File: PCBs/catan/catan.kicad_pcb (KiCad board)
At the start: 2 copper layers, 95.3 x 110 mm, 65 parts, among them J1 Conn_01x04_Female, J2 Conn_01x06_Male, SW1 SW_MEC_5E, SW10 SW_MEC_5E, SW11 SW_MEC_5E, SW2 SW_MEC_5E, SW3 SW_MEC_5E, SW4 SW_MEC_5E, SW5 SW_MEC_5E, SW6 SW_MEC_5E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

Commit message: wire buttons
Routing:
- net Net-(R25-Pad2): track 3.07 -> 84.9 mm
- net Net-(R24-Pad2): track 2.54 -> 59.8 mm
- net Net-(R3-Pad2): track 4.34 -> 57.9 mm
- net Net-(R4-Pad2): track 3.44 -> 54.3 mm
- net Net-(R5-Pad2): track 4.86 -> 39.1 mm
- net Net-(R6-Pad2): track 2.54 -> 29.4 mm
- net Net-(R23-Pad2): track 3.59 -> 28.5 mm
- net Net-(R27-Pad2): track 3.33 -> 27.6 mm
- net GND: track 633.6 -> 649.8 mm
- net Net-(R7-Pad2): track 6.40 -> 18.8 mm
- net Net-(R26-Pad2): track 3.33 -> 15.0 mm
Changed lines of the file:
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@@
     (thickness 1.6)
     (drawings 12)
-    (tracks 281)
+    (tracks 330)
     (zones 0)
     (modules 65)
@@
   (segment (start 139.7 116.205) (end 134.129999 110.634999) (width 0.25) (layer B.Cu) (net 1))
   (segment (start 119.38 93.345) (end 131.445 93.345) (width 0.25) (layer B.Cu) (net 1))
+  (segment (start 102.87 92.075) (end 102.87 94.615) (width 0.25) (layer B.Cu) (net 1))
+  (segment (start 102.87 94.615) (end 102.87 97.155) (width 0.25) (layer B.Cu) (net 1))
+  (segment (start 102.87 97.155) (end 102.87 99.695) (width 0.25) (layer B.Cu) (net 1))
+  (segment (start 103.995001 103.649999) (end 102.87 104.775) (width 0.25) (layer B.Cu) (net 1))
+  (segment (start 103.995001 100.820001) (end 103.995001 103.649999) (width 0.25) (layer B.Cu) (net 1))
+  (segment (start 102.87 99.695) (end 103.995001 100.820001) (width 0.25) (layer B.Cu) (net 1))
+  (segment (start 110.49 92.075) (end 110.49 94.615) (width 0.25) (layer B.Cu) (net 1))
   (segment (start 90.805 63.5) (end 90.805 71.12) (width 0.25) (layer B.Cu) (net 2))
   (segment (start 86.995 74.93) (end 90.805 71.12) (width 0.25) (layer B.Cu) (net 2))
@@
   (segment (start 158.115 85.725) (end 159.385 86.995) (width 0.25) (layer B.Cu) (net 41))
   (segment (start 158.115 83.185) (end 158.115 85.725) (width 0.25) (layer B.Cu) (net 41))
+  (segment (start 112.000001 77.229999) (end 110.49 78.74) (width 0.25) (layer F.Cu) (net 41))
+  (segment (start 136.065001 77.229999) (end 112.000001 77.229999) (width 0.25) (layer F.Cu) (net 41))
+  (segment (start 145.830002 86.995) (end 136.065001 77.229999) (width 0.25) (layer F.Cu) (net 41))
+  (segment (start 159.385 86.995) (end 145.830002 86.995) (width 0.25) (layer F.Cu) (net 41))
   (segment (start 158.115 74.295) (end 158.75 74.93) (width 0.25) (layer B.Cu) (net 42))
   (segment (start 158.115 71.755) (end 158.115 74.295) (width 0.25) (layer B.Cu) (net 42))
+  (segment (start 155.970002 76.2) (end 110.49 76.2) (width 0.25) (layer F.Cu) (net 42))
+  (segment (start 158.115 74.055002) (end 155.970002 76.2) (width 0.25) (layer F.Cu) (net 42))
+  (segment (start 158.115 71.755) (end 158.115 74.055002) (width 0.25) (layer F.Cu) (net 42))
   (segment (start 137.16 59.055) (end 139.7 61.595) (width 0.25) (layer B.Cu) (net 43))
   (segment (start 137.16 57.785) (end 137.16 59.055) (width 0.25) (layer B.Cu) (net 43))
+  (segment (start 139.7 61.595) (end 127.635 73.66) (width 0.25) (layer F.Cu) (net 43))
+  (segment (start 127.635 73.66) (end 110.49 73.66) (width 0.25) (layer F.Cu) (net 43))
   (segment (start 121.92 50.165) (end 119.38 50.165) (width 0.25) (layer B.Cu) (net 44))
+  (segment (start 119.139999 62.470001) (end 110.49 71.12) (width 0.25) (layer F.Cu) (net 44))
+  (segment (start 119.139999 58.264999) (end 119.139999 62.470001) (width 0.25) (layer F.Cu) (net 44))
+  (segment (start 121.034997 56.370001) (end 119.139999 58.264999) (width 0.25) (layer F.Cu) (net 44))
+  (segment (start 121.825001 56.370001) (end 121.034997 56.370001) (width 0.25) (layer F.Cu) (net 44))
+  (segment (start 122.769999 51.014999) (end 122.769999 55.425003) (width 0.25) (layer F.Cu) (net 44))
+  (segment (start 122.769999 55.425003) (end 121.825001 56.370001) (width 0.25) (layer F.Cu) (net 44))
+  (segment (start 121.92 50.165) (end 122.769999 51.014999) (width 0.25) (layer F.Cu) (net 44))
   (segment (start 100.965 64.135) (end 104.14 60.96) (width 0.25) (layer B.Cu) (net 45))
   (segment (start 99.06 64.135) (end 100.965 64.135) (width 0.25) (layer B.Cu) (net 45))
+  (segment (start 101.744999 69.994999) (end 102.87 71.12) (width 0.25) (layer F.Cu) (net 45))
+  (segment (start 101.744999 68.039999) (end 101.744999 69.994999) (width 0.25) (layer F.Cu) (net 45))
+  (segment (start 102.619997 67.165001) (end 101.744999 68.039999) (width 0.25) (layer F.Cu) (net 45))
+  (segment (start 103.930001 67.165001) (end 102.619997 67.165001) (width 0.25) (layer F.Cu) (net 45))
+  (segment (start 104.14 66.955002) (end 103.930001 67.165001) (width 0.25) (layer F.Cu) (net 45))
+  (segment (start 104.14 60.96) (end 104.14 66.955002) (width 0.25) (layer F.Cu) (net 45))
   (segment (start 90.17 93.345) (end 92.71 95.885) (width 0.25) (layer B.Cu) (net 61))
+  (segment (start 91.345001 85.184999) (end 102.87 73.66) (width 0.25) (layer F.Cu) (net 61))
+  (segment (start 91.345001 92.169999) (end 91.345001 85.184999) (width 0.25) (layer F.Cu) (net 61))
+  (segment (start 90.17 93.345) (end 91.345001 92.169999) (width 0.25) (layer F.Cu) (net 61))
   (segment (start 110.49 116.205) (end 110.49 118.745) (width 0.25) (layer B.Cu) (net 62))
+  (segment (start 102.87 76.2) (end 94.615 84.455) (width 0.25) (layer F.Cu) (net 62))
+  (segment (start 105.739989 113.994989) (end 110.49 118.745) (width 0.25) (layer F.Cu) (net 62))
+  (segment (start 97.739987 113.994989) (end 105.739989 113.994989) (width 0.25) (layer F.Cu) (net 62))
+  (segment (start 94.615 110.870002) (end 97.739987 113.994989) (width 0.25) (layer F.Cu) (net 62))
+  (segment (start 94.615 84.455) (end 94.615 110.870002) (width 0.25) (layer F.Cu) (net 62))
   (segment (start 146.05 117.475) (end 146.05 118.745) (width 0.25) (layer B.Cu) (net 63))
   (segment (start 147.32 116.205) (end 146.05 117.475) (width 0.25) (layer B.Cu) (net 63))
+  (segment (start 101.744999 79.865001) (end 102.87 78.74) (width 0.25) (layer F.Cu) (net 63))
+  (segment (start 102.474998 90.805) (end 101.744999 90.075001) (width 0.25) (layer F.Cu) (net 63))
+  (segment (start 101.744999 90.075001) (end 101.744999 79.865001) (width 0.25) (layer F.Cu) (net 63))
+  (segment (start 110.885002 90.805) (end 102.474998 90.805) (width 0.25) (layer F.Cu) (net 63))
+  (segment (start 112.745003 88.944999) (end 110.885002 90.805) (width 0.25) (layer F.Cu) (net 63))
+  (segment (start 137.245411 88.944999) (end 112.745003 88.944999) (width 0.25) (layer F.Cu) (net 63))
+  (segment (start 146.05 97.749588) (end 137.245411 88.944999) (width 0.25) (layer F.Cu) (net 63))
+  (segment (start 146.05 118.745) (end 146.05 97.749588) (width 0.25) (layer F.Cu) (net 63))
   (segment (start 120.015 100.965) (end 119.38 100.965) (width 0.25) (layer B.Cu) (net 64))
   (segment (start 121.92 99.06) (end 120.015 100.965) (width 0.25) (layer B.Cu) (net 64))
+  (segment (start 111.125 99.06) (end 110.49 99.695) (width 0.25) (layer F.Cu) (net 64))
+  (segment (start 121.92 99.06) (end 111.125 99.06) (width 0.25) (layer F.Cu) (net 64))
   (segment (start 132.08 100.965) (end 131.445 100.965) (width 0.25) (layer B.Cu) (net 65))
   (segment (start 133.985 99.06) (end 132.08 100.965) (width 0.25) (layer B.Cu) (net 65))
+  (segment (start 132.08 97.155) (end 110.49 97.155) (width 0.25) (layer F.Cu) (net 65))
+  (segment (start 133.985 99.06) (end 132.08 97.155) (width 0.25) (layer F.Cu) (net 65))
   (segment (start 103.995001 88.409999) (end 102.87 89.535) (width 0.25) (layer F.Cu) (net 69))
   (segment (start 103.995001 69.705001) (end 103.995001 88.409999) (width 0.25) (layer F.Cu) (net 69))

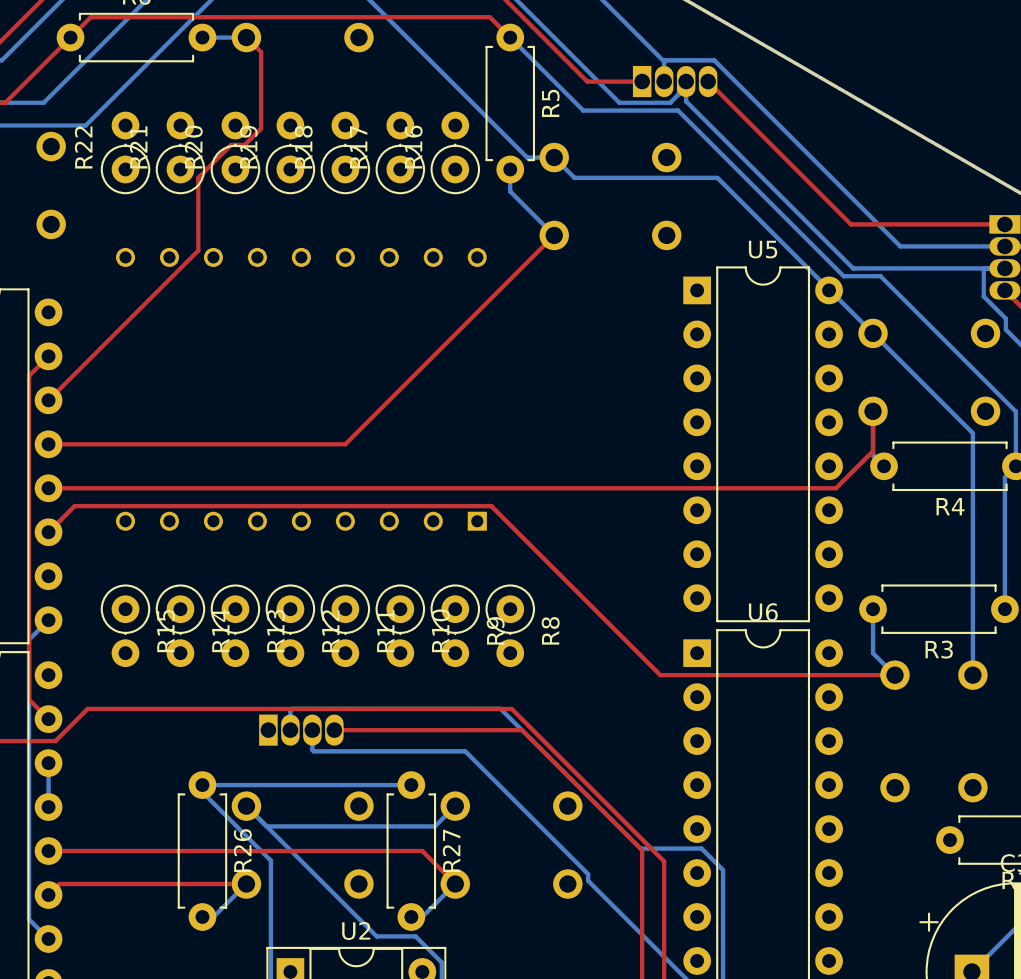
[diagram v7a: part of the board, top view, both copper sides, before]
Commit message: wire segment display to registers
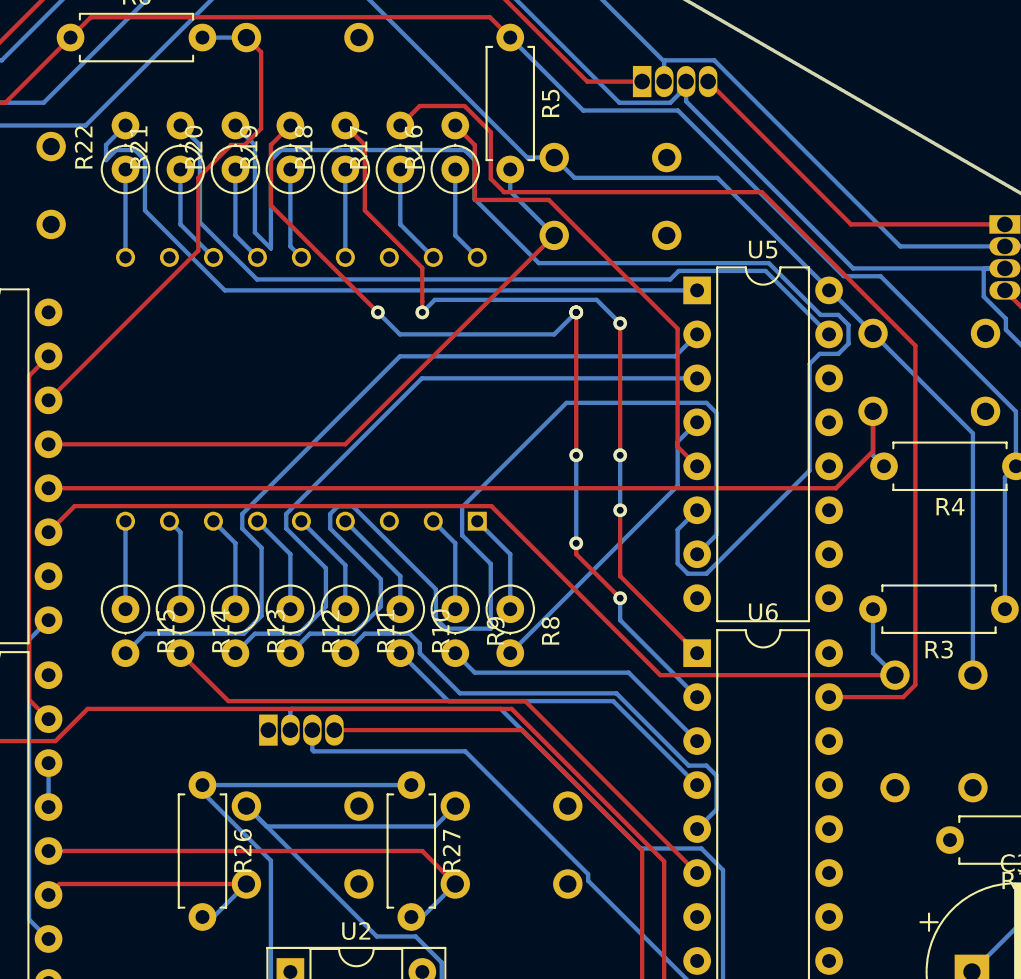
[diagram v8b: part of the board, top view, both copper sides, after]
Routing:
- net Net-(R20-Pad2): track 0.00 -> 76.0 mm
- net Net-(R17-Pad2): track 0.00 -> 62.4 mm
- net Net-(R12-Pad2): track 0.00 -> 60.1 mm
- net Net-(R19-Pad2): track 0.00 -> 51.4 mm, vias 0 -> 6
- net Net-(R18-Pad2): track 0.00 -> 45.8 mm, vias 0 -> 4
- net Net-(R15-Pad2): track 0.00 -> 45.7 mm
- net Net-(R21-Pad2): track 0.00 -> 45.5 mm
- net Net-(R22-Pad2): track 0.00 -> 41.9 mm
- net Net-(R13-Pad2): track 0.00 -> 39.6 mm
- net Net-(R14-Pad2): track 0.00 -> 35.1 mm
- net Net-(R11-Pad2): track 0.00 -> 29.2 mm
- net Net-(R16-Pad2): track 0.00 -> 28.0 mm
- net Net-(R10-Pad2): track 0.00 -> 20.3 mm
- net Net-(R8-Pad2): track 0.00 -> 17.8 mm
- net Net-(R9-Pad2): track 0.00 -> 16.1 mm
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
